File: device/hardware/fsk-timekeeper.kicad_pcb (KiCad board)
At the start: 2 copper layers, 92 x 57 mm, 24 parts, among them J1 SENSOR, SW1 SW_SPST, U1 SuperMini nRF52840, U2 Ai-Thinker Ra-01SH, U3 TPS61040DBV

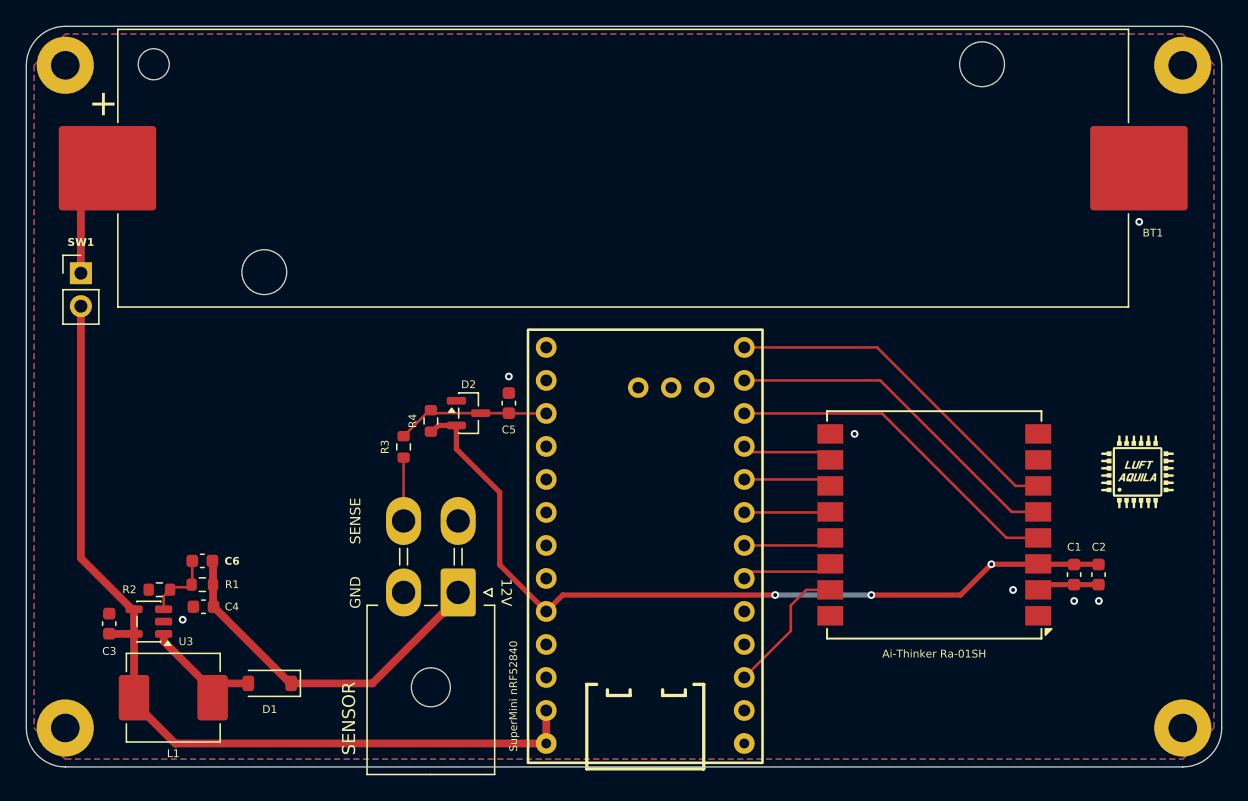
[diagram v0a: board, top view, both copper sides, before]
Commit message: add: GPS on the master — ATGM336H, PPS clock calibration, new pin map
Hardware: ATGM336H breakout (U4, master boards only) with a project-local symbol
and footprint; SENSOR moves to P1.13, GPS PPS/RXD/TXD take P0.09/P1.11/P0.10.
Firmware: pin map in config.h; board.c clears UICR.NFCPINS.PROTECT once per
board (readback-guarded reset); the idle SENSOR capture channel captures PPS
on the master; gps.c drives UARTE0 (NMEA, GGA+RMC via $PCAS03), parses fix,
satellites and UTC, and estimates the HFXO error from an 8-64 s window of
gated PPS edges. Reported on the new `P` line (~1 Hz, also in ?STATUS); wire
ticks stay raw, the console applies the correction.

Co-Authored-By: Claude Fable 5.1 <noreply@anthropic.com>
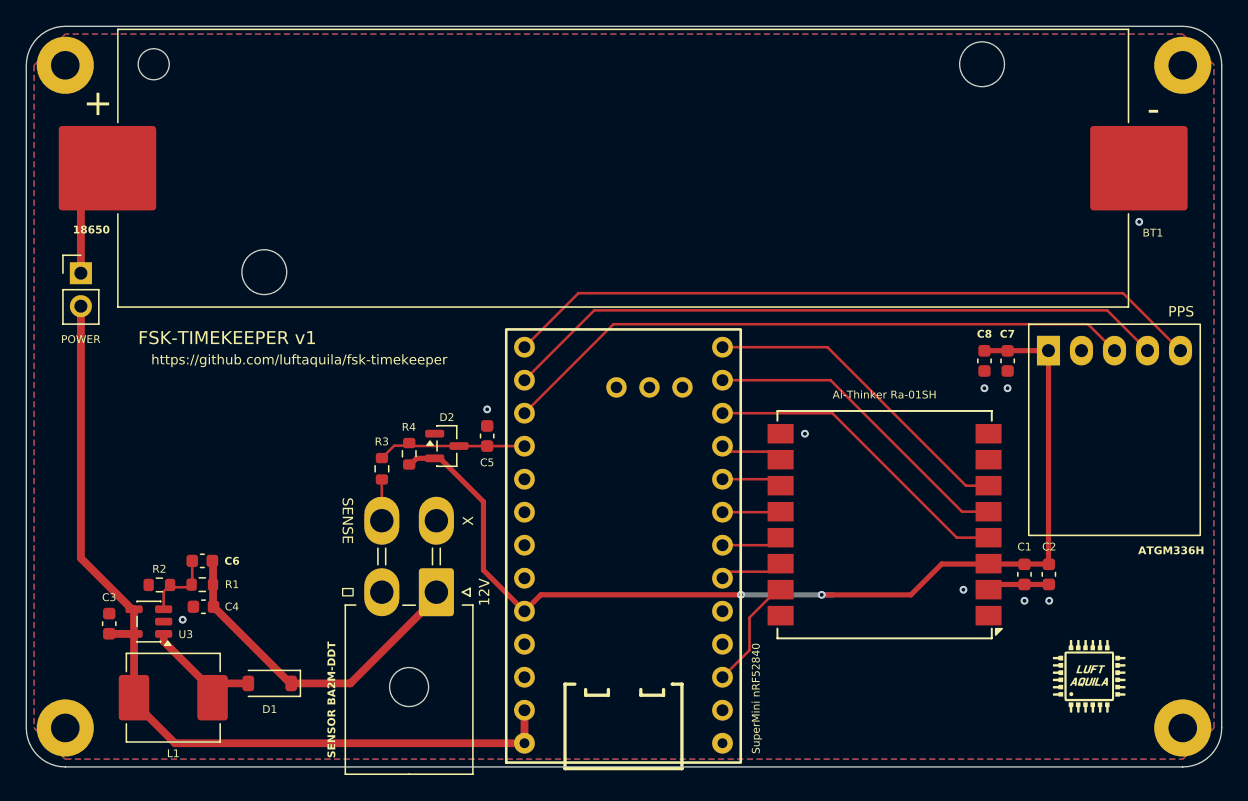
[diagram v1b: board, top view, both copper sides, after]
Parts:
- added C7: 100nF, Capacitor_SMD:C_0603_1608Metric, F.Cu at (176.7, 95.3)
- added C8: 10uF, Capacitor_SMD:C_0603_1608Metric, F.Cu at (174.9, 95.3)
- added U4: ATGM336H, lib:ATGM336H_GPS_Module, F.Cu at (184.9, 94.5)
- J1: value SENSOR -> SENSOR BA2M-DDT
- SW1: value SW_SPST -> POWER
- moved G*** 16.2 mm to (183.0, 119.5)
- moved C1 3.82 mm to (178.0, 111.7)
- moved C2 3.82 mm to (179.9, 111.7)
- moved U2 3.82 mm to (167.2, 107.9)
- moved C5 3.03 mm to (136.6, 101.1)
- moved D2 3.03 mm to (133.5, 101.8)
- moved R4 3.03 mm to (130.6, 102.4)
- moved R3 2.37 mm to (128.5, 103.6)
- moved J1 1.68 mm to (132.7, 113.1)
- moved U1 1.68 mm to (154.7, 124.7)
- moved R2 0.37 mm to (111.4, 112.5)
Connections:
- U1 pad 21: unconnected-(U1-P1.13-LF-Pad21) -> /SENSOR
- U1 pad 22: /SENSOR -> /RX
- U1 pad 23: unconnected-(U1-P0.10-LF-Pad23) -> /TX
- U1 pad 24: unconnected-(U1-P0.09-LF-Pad24) -> /PPS
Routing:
- net /PPS: track 0.00 -> 54.0 mm
- net /TX: track 0.00 -> 51.5 mm
- net /RX: track 0.00 -> 49.1 mm
- net +3.3V: track 63.3 -> 81.4 mm, vias 3 -> 2
- net /TXEN: track 26.8 -> 24.7 mm
- net /NRST: track 26.6 -> 24.4 mm
- net /DIO1: track 27.0 -> 24.9 mm
- net /NSS: track 10.9 -> 9.11 mm
- net /SENSE: track 4.88 -> 3.18 mm
- net +BATT: track 69.8 -> 68.1 mm
- net +12V: track 28.0 -> 26.4 mm
- net /RXEN: track 6.83 -> 5.57 mm
- net /SCK: track 6.64 -> 5.45 mm
- net /MOSI: track 7.09 -> 5.98 mm
- net GND: vias 7 -> 9
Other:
- board text added: "-"
- board text added: "18650"
- board text added: "FSK-TIMEKEEPER v1"
- board text added: "PPS"
- board text added: "X"
- board text added: "https://github.com/luftaquila/fsk-timekeeper"
- board text added: "⏚"
- board text removed: "GND"

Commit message: fix(hardware): finalize radio wiring, PCB routing and fabrication outputs
Reorganized from:
- 0e2d74b fix: leave the Ra-01SH TXEN and RXEN pins unconnected
- dd02dfc add: stitch the GND pours with vias
- 162bb38 fix: exclude the known ERC items so the check can pass
- 6ef263c fix: remove the track pieces that lie inside pads
- 0b254e7 fix: keep hand-soldered parts out of the JLCPCB BOM and CPL
- 47fa68c add: JLCPCB fabrication files from the assembly plugin

Co-Authored-By: Claude Opus 5.5 <noreply@anthropic.com>
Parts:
- J1: value SENSOR BA2M-DDT -> SENSOR
- SW1: value POWER -> SW_SPST
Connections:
- U1 pad 11: /TXEN -> unconnected-(U1-P1.04-LF-Pad11)
- U1 pad 8: /RXEN -> unconnected-(U1-P0.24-Pad8)
- U2 pad 11: /RXEN -> unconnected-(U2-DIO5-Pad11)
- U2 pad 5: /TXEN -> unconnected-(U2-DIO0-Pad5)
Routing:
- net /TXEN: track 24.7 -> 0.00 mm
- net /RXEN: track 5.57 -> 0.00 mm
- net Net-(BT1-+): track 8.93 -> 6.03 mm
- net /BUSY: track 6.65 -> 4.33 mm
- net /MOSI: track 5.98 -> 4.25 mm
- net +3.3V: track 81.4 -> 79.7 mm
- net /MISO: track 6.43 -> 4.79 mm
- net +BATT: track 68.1 -> 67.4 mm
- net +12V: track 26.4 -> 25.7 mm
- net /NSS: track 9.11 -> 8.49 mm
- net Net-(U3-FB): track 5.73 -> 5.13 mm
- net Net-(D1-A): track 8.12 -> 7.55 mm
- net GND: vias 9 -> 69

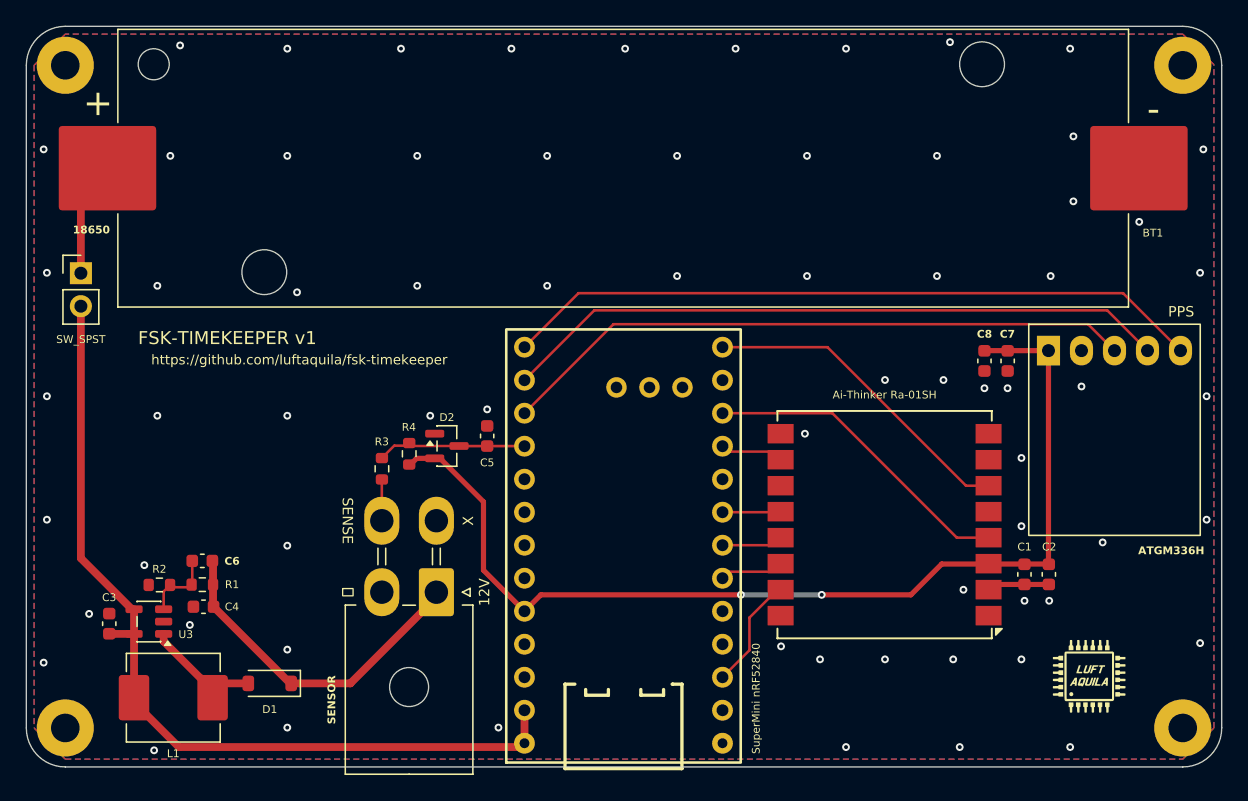
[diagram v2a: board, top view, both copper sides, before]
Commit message: fix(hardware): match field-board J1 pinout and revise boost layout
Reorganized from:
- be4e238 fix: match J1 to the field board pinout and tighten the boost layout

Co-Authored-By: Claude Opus 5.5 <noreply@anthropic.com>
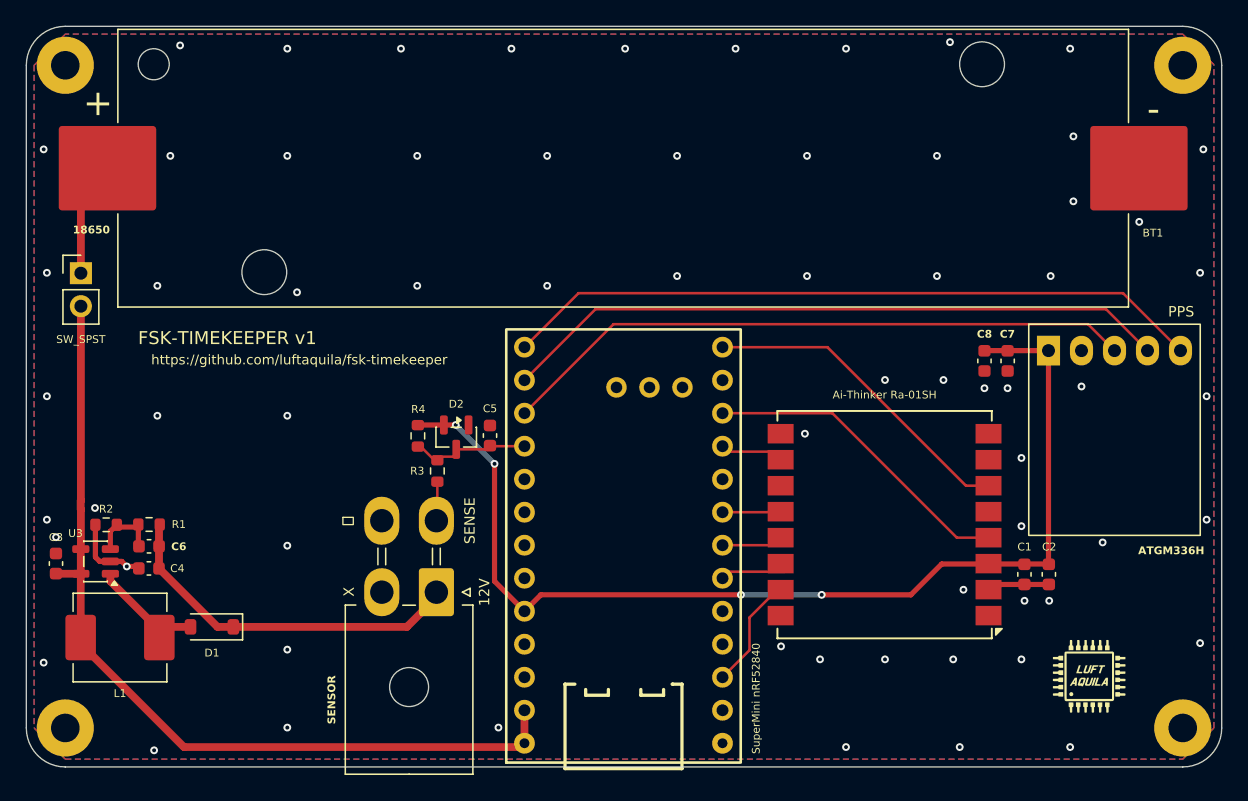
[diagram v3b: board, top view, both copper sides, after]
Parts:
- moved D1 6.22 mm to (115.5, 115.8)
- moved L1 6.18 mm to (108.4, 116.6)
- moved R2 6.18 mm to (107.3, 107.9)
- moved C3 6.18 mm to (103.4, 110.9)
- moved R1 6.18 mm to (110.6, 107.9)
- moved U3 6.18 mm to (106.5, 110.7)
- moved C4 5.13 mm to (110.6, 111.2)
- moved R3 4.27 mm to (132.8, 103.8)
- moved C6 4.25 mm to (110.6, 109.5)
- moved R4 1.53 mm to (131.3, 101.0), turned to 90 degrees
- moved D2 0.99 mm to (134.2, 101.2), turned to -90 degrees
- moved C5 0.22 mm to (136.8, 101.0)
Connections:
- J1 pad 2: GND -> unconnected-(J1-Pin_2-Pad2)
- J1 pad 3: unconnected-(J1-Pin_3-Pad3) -> /SENSE
- J1 pad 4: /SENSE -> GND
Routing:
- net GND: track 4.21 -> 10.2 mm, vias 69 -> 67
- net /SENSOR: track 11.3 -> 7.80 mm
- net +3.3V: track 79.7 -> 82.5 mm, vias 2 -> 4
- net +12V: track 25.7 -> 27.5 mm
- net Net-(D1-A): track 7.55 -> 8.30 mm
